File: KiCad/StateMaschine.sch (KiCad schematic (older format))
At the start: 36 parts

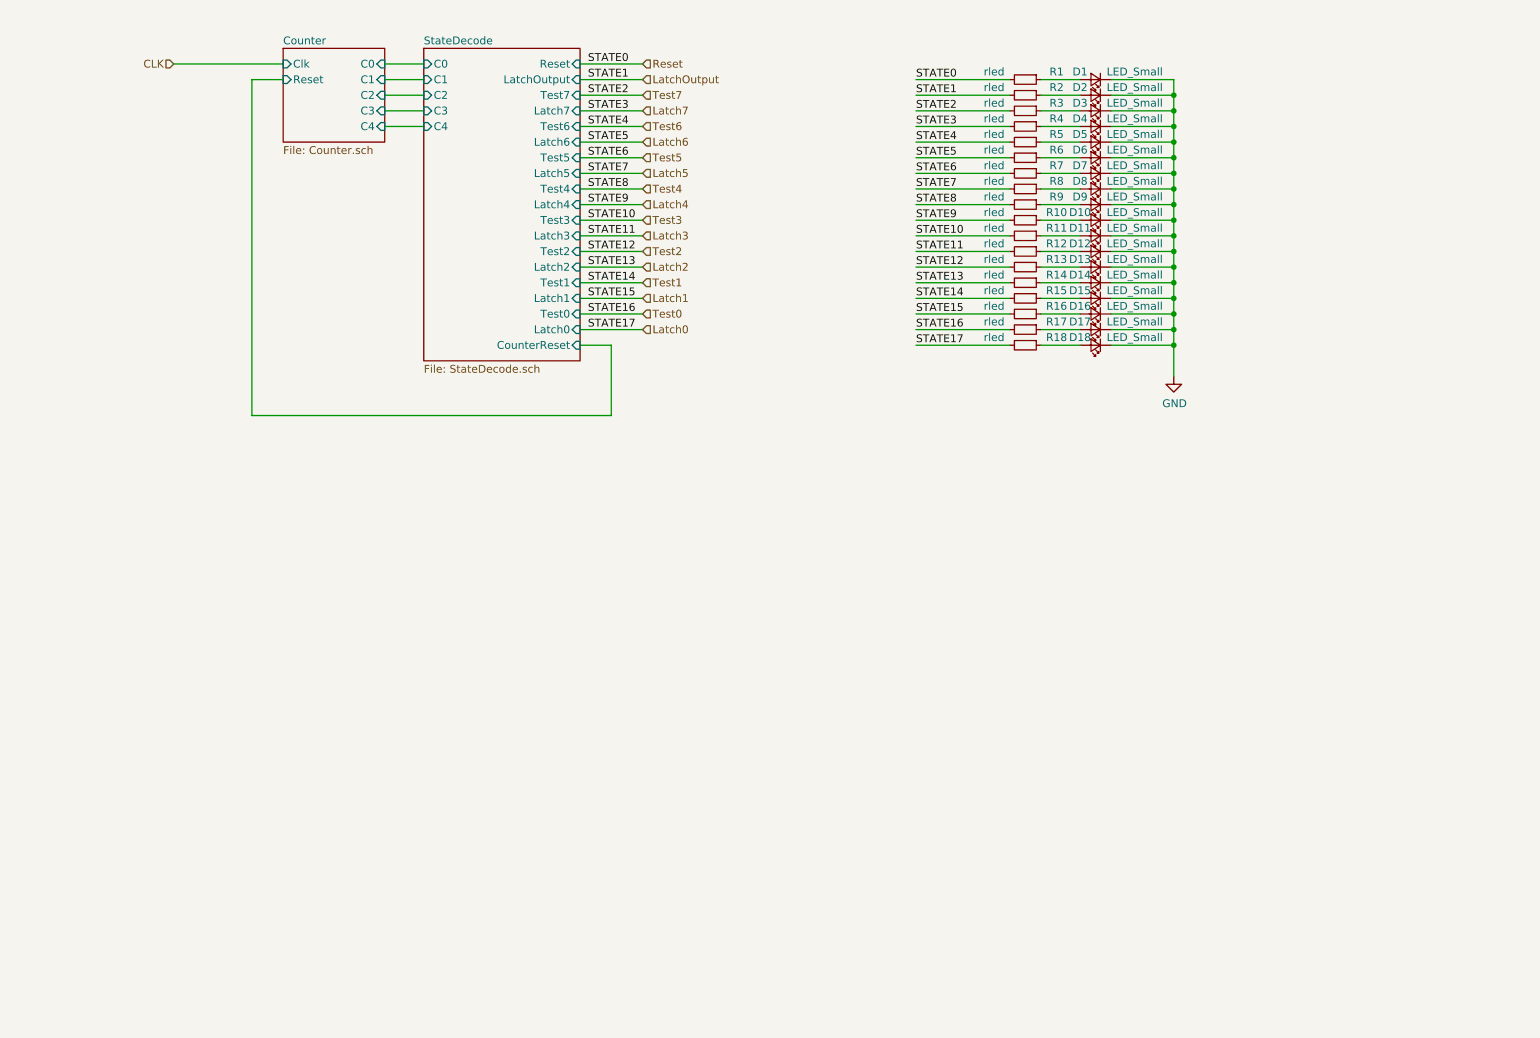
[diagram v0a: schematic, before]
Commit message: Schematic Update First Draft, ERC Passed
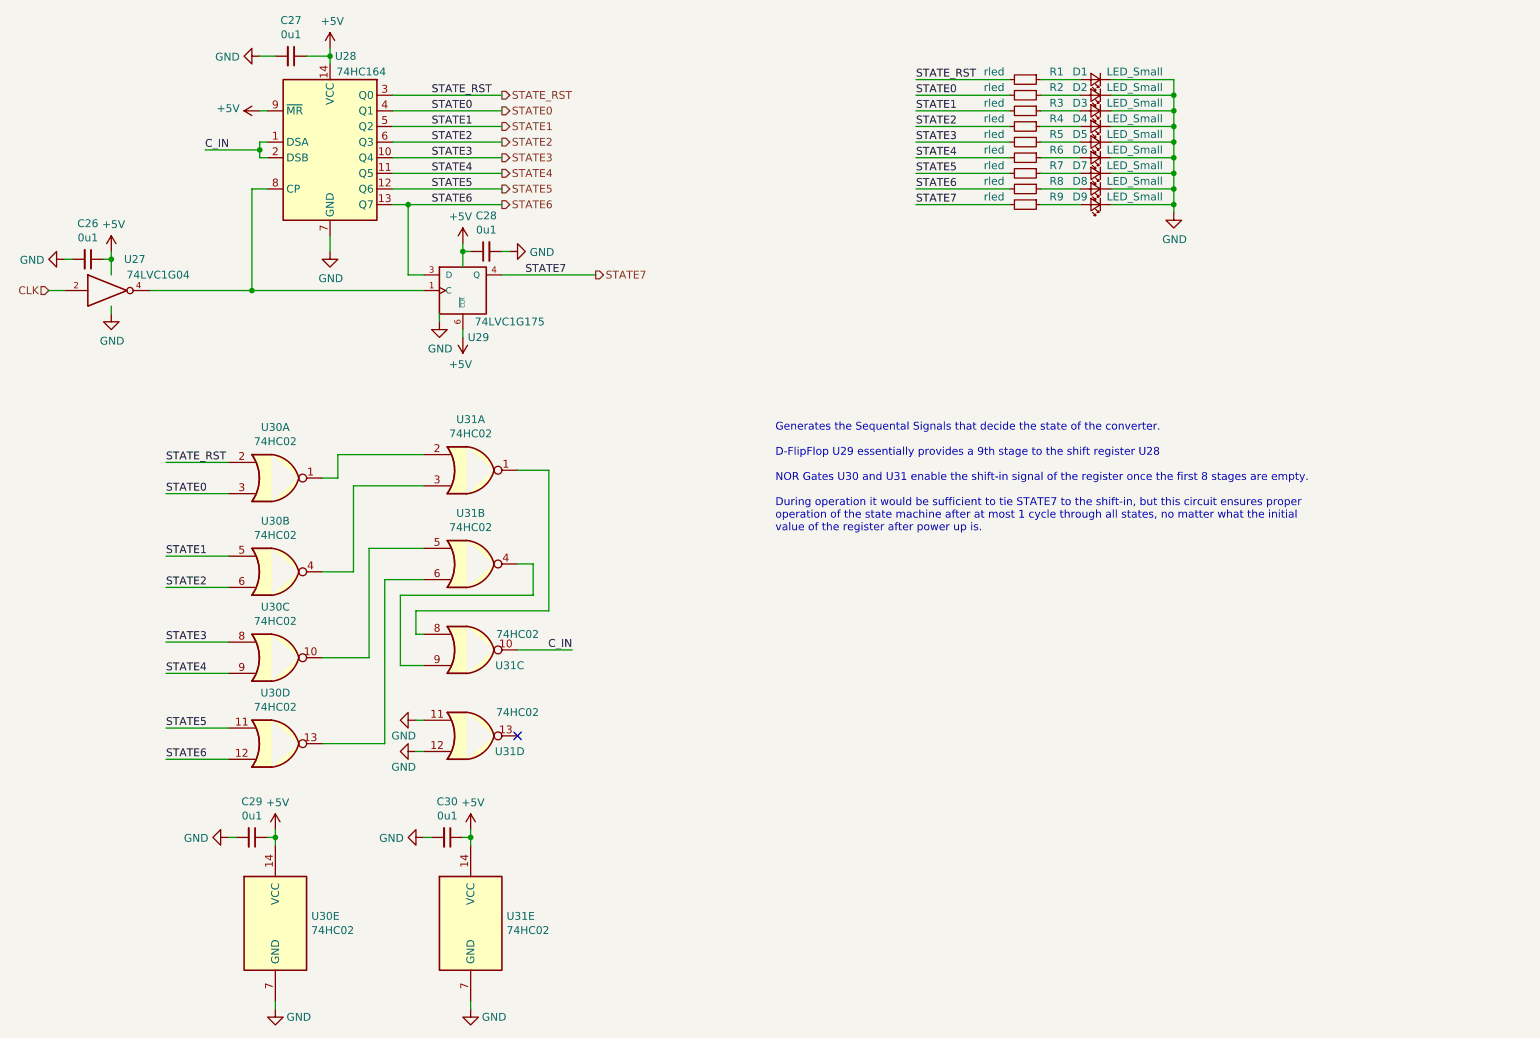
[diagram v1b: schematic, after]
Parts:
- removed D10, D11, D12, D13, D14, D15, D16, D17, D18: LED_Small, LED_SMD:LED_0805_2012Metric, symbol Device:LED_Small
- removed R10, R11, R12, R13, R14, R15, R16, R17, R18: rled, Resistor_SMD:R_0603_1608Metric, symbol Device:R_Small
- added C26, C27, C28, C29, C30: 0u1, Capacitor_SMD:C_0603_1608Metric, symbol Device:C_Small
- added U27: 74LVC1G04, Package_TO_SOT_SMD:SOT-353_SC-70-5, symbol 74xGxx:74LVC1G04
- added U28: 74HC164, Package_SO:SOIC-16_3.9x9.9mm_P1.27mm, symbol 74xx:74HC164
- added U29: 74LVC1G175, Package_TO_SOT_SMD:SOT-363_SC-70-6, symbol 74xGxx:74LVC1G175
- added U30, U31: 74HC02, Package_SO:SOIC-14_3.9x8.7mm_P1.27mm, symbol 74xx:74HC02
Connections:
- net CLK: now also U27.2
- net GND: now also C26.2, C27.2, C28.2, C29.2, C30.2, U27.3 (GND), U28.7 (GND), U29.2 (GND), U30.7 (GND), U31.11, U31.12, U31.7 (GND)
- net Latch5 renamed STATE6
- net STATE6: now also U28.13 (Q7), U29.3 (D), U30.12
- net Latch6 renamed STATE4
- net STATE4: now also U28.11 (Q5), U30.9
- net Latch7 renamed STATE2
- net STATE2: now also U28.6 (Q3), U30.6
- net LatchOutput renamed STATE0
- net STATE0: now also U28.4 (Q1), U30.3
- net Reset renamed STATE_RST
- net STATE_RST: now also U28.3 (Q0), U30.2
- net Test4 renamed STATE7
- net STATE7: now also U29.4 (Q)
- net Test5 renamed STATE5
- net STATE5: now also U28.12 (Q6), U30.11
- net Test6 renamed STATE3
- net STATE3: now also U28.10 (Q4), U30.8
- net Test7 renamed STATE1
- net STATE1: now also U28.5 (Q2), U30.5
- new net: U27.4, U28.8 (CP), U29.1 (C)
- new net: U30.1, U31.2
- new net: U30.4, U31.3
- new net: U30.10, U31.5
- new net: U30.13, U31.6
- new net: U31.1, U31.8
- new net: U31.4, U31.9
- new net +5V: C26.1, C27.1, C28.1, C29.1, C30.1, U27.5 (VCC), U28.14 (VCC), U28.9 (~MR), U29.5 (VCC), U29.6 (~CLR), U30.14 (VCC), U31.14 (VCC)
- new net C_IN: U28.1 (DSA), U28.2 (DSB), U31.10
- no-connect marks 0 -> 1
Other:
- note added: "Generates the Sequental Signals that decide the state of the converter.\n\nD-FlipFlop U29 essentially provides a 9th stage to the shift register U28\n\nNOR Gates U30 and U31 enable the shift-in signal of the register once the first 8 stages are empty. \n\nDuring operation it would be sufficient to tie STATE7 to the shift-in, but this circuit ensures proper \noperation of the state machine after a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"

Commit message: First part placement
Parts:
- D1, D2, D3, D4, D5, D6, D7, D8, D9: footprint LED_SMD:LED_0805_2012Metric -> LED_SMD:LED_0603_1608Metric
- U28: footprint Package_SO:SOIC-16_3.9x9.9mm_P1.27mm -> Package_SO:SOIC-14_3.9x8.7mm_P1.27mm
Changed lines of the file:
@@
 F 0 "D1" H 8750 1550 50  0000 C CNN
 F 1 "LED_Small" H 8400 1550 50  0000 C CNN
-F 2 "LED_SMD:LED_0805_2012Metric" V 8650 1600 50  0001 C CNN
+F 2 "LED_SMD:LED_0603_1608Metric" V 8650 1600 50  0001 C CNN
 F 3 "~" V 8650 1600 50  0001 C CNN
 	1    8650 1600
@@
 F 0 "D2" H 8750 1650 50  0000 C CNN
 F 1 "LED_Small" H 8400 1650 50  0000 C CNN
-F 2 "LED_SMD:LED_0805_2012Metric" V 8650 1700 50  0001 C CNN
+F 2 "LED_SMD:LED_0603_1608Metric" V 8650 1700 50  0001 C CNN
 F 3 "~" V 8650 1700 50  0001 C CNN
 	1    8650 1700
@@
 F 0 "D3" H 8750 1750 50  0000 C CNN
 F 1 "LED_Small" H 8400 1750 50  0000 C CNN
-F 2 "LED_SMD:LED_0805_2012Metric" V 8650 1800 50  0001 C CNN
+F 2 "LED_SMD:LED_0603_1608Metric" V 8650 1800 50  0001 C CNN
 F 3 "~" V 8650 1800 50  0001 C CNN
 	1    8650 1800
@@
 F 0 "D4" H 8750 1850 50  0000 C CNN
 F 1 "LED_Small" H 8400 1850 50  0000 C CNN
-F 2 "LED_SMD:LED_0805_2012Metric" V 8650 1900 50  0001 C CNN
+F 2 "LED_SMD:LED_0603_1608Metric" V 8650 1900 50  0001 C CNN
 F 3 "~" V 8650 1900 50  0001 C CNN
 	1    8650 1900
@@
 F 0 "D5" H 8750 1950 50  0000 C CNN
 F 1 "LED_Small" H 8400 1950 50  0000 C CNN
-F 2 "LED_SMD:LED_0805_2012Metric" V 8650 2000 50  0001 C CNN
+F 2 "LED_SMD:LED_0603_1608Metric" V 8650 2000 50  0001 C CNN
 F 3 "~" V 8650 2000 50  0001 C CNN
 	1    8650 2000
@@
 F 0 "D6" H 8750 2050 50  0000 C CNN
 F 1 "LED_Small" H 8400 2050 50  0000 C CNN
-F 2 "LED_SMD:LED_0805_2012Metric" V 8650 2100 50  0001 C CNN
+F 2 "LED_SMD:LED_0603_1608Metric" V 8650 2100 50  0001 C CNN
 F 3 "~" V 8650 2100 50  0001 C CNN
 	1    8650 2100
@@
 F 0 "D7" H 8750 2150 50  0000 C CNN
 F 1 "LED_Small" H 8400 2150 50  0000 C CNN
-F 2 "LED_SMD:LED_0805_2012Metric" V 8650 2200 50  0001 C CNN
+F 2 "LED_SMD:LED_0603_1608Metric" V 8650 2200 50  0001 C CNN
 F 3 "~" V 8650 2200 50  0001 C CNN
 	1    8650 2200
@@
 F 0 "D8" H 8750 2250 50  0000 C CNN
 F 1 "LED_Small" H 8400 2250 50  0000 C CNN
-F 2 "LED_SMD:LED_0805_2012Metric" V 8650 2300 50  0001 C CNN
+F 2 "LED_SMD:LED_0603_1608Metric" V 8650 2300 50  0001 C CNN
 F 3 "~" V 8650 2300 50  0001 C CNN
 	1    8650 2300
@@
 F 0 "D9" H 8750 2350 50  0000 C CNN
 F 1 "LED_Small" H 8400 2350 50  0000 C CNN
-F 2 "LED_SMD:LED_0805_2012Metric" V 8650 2400 50  0001 C CNN
+F 2 "LED_SMD:LED_0603_1608Metric" V 8650 2400 50  0001 C CNN
 F 3 "~" V 8650 2400 50  0001 C CNN
 	1    8650 2400
@@
 F 0 "U28" H 3850 2550 50  0000 C CNN
 F 1 "74HC164" H 3950 2450 50  0000 C CNN
-F 2 "Package_SO:SOIC-16_3.9x9.9mm_P1.27mm" H 4650 1700 50  0001 C CNN
+F 2 "Package_SO:SOIC-14_3.9x8.7mm_P1.27mm" H 4650 1700 50  0001 C CNN
 F 3 "https://assets.nexperia.com/documents/data-sheet/74HC_HCT164.pdf" H 4650 1700 50  0001 C CNN
 	1    3750 2000

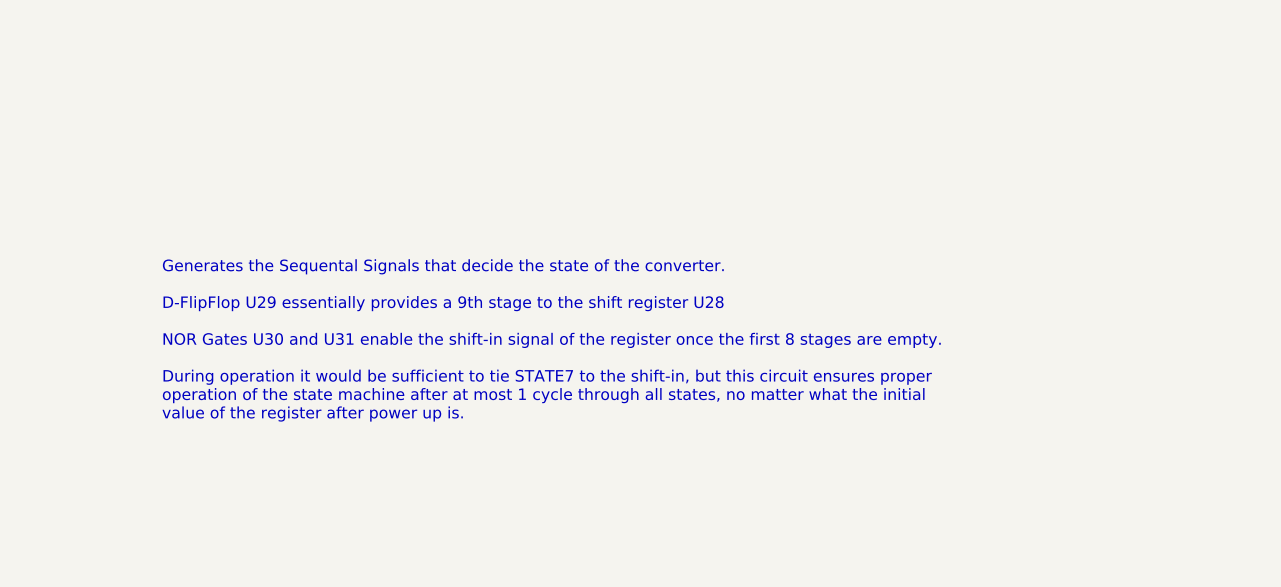
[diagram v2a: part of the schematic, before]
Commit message: First Layout (All Connected, passes DRC)
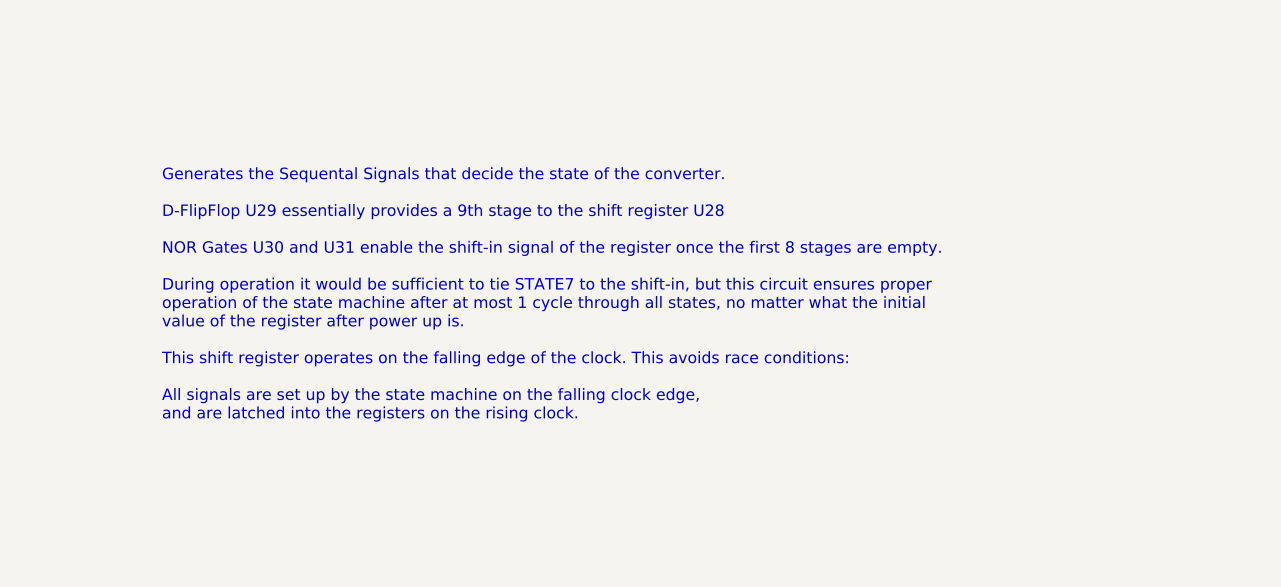
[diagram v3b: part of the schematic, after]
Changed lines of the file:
@@
 	3300 2050 3300 2100
 Text Notes 6600 4500 0    50   ~ 0
-Generates the Sequental Signals that decide the state of the converter.\n\nD-FlipFlop U29 essentially provides a 9th stage to the shift register U28\n\nNOR Gates U30 and U31 enable the shift-in signal of the register once the first 8 stages are empty. \n\nDuring operation it would be sufficient to tie STATE7 to the shift-in, but this circuit ensures proper \noperation of the state machine after at most 1 cycle through all states, no matter what the initial\nvalue of the register after power up is.
+Generates the Sequental Signals that decide the state of the converter.\n\nD-FlipFlop U29 essentially provides a 9th stage to the shift register U28\n\nNOR Gates U30 and U31 enable the shift-in signal of the register once the first 8 stages are empty. \n\nDuring operation it would be sufficient to tie STATE7 to the shift-in, but this circuit ensures proper \noperation of the state machine after at most 1 cycle through all states, no matter what the initial\nvalue of the register after power up is.\n\nThis shift register operates on the falling edge of the clock. This avoids race conditions:\n\nAll signals are set up by the state machine on the falling clock edge,\nand are latched into the registers on the rising clock.
 $EndSCHEMATC
